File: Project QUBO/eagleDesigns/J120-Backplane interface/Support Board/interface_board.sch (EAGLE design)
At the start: 5 parts

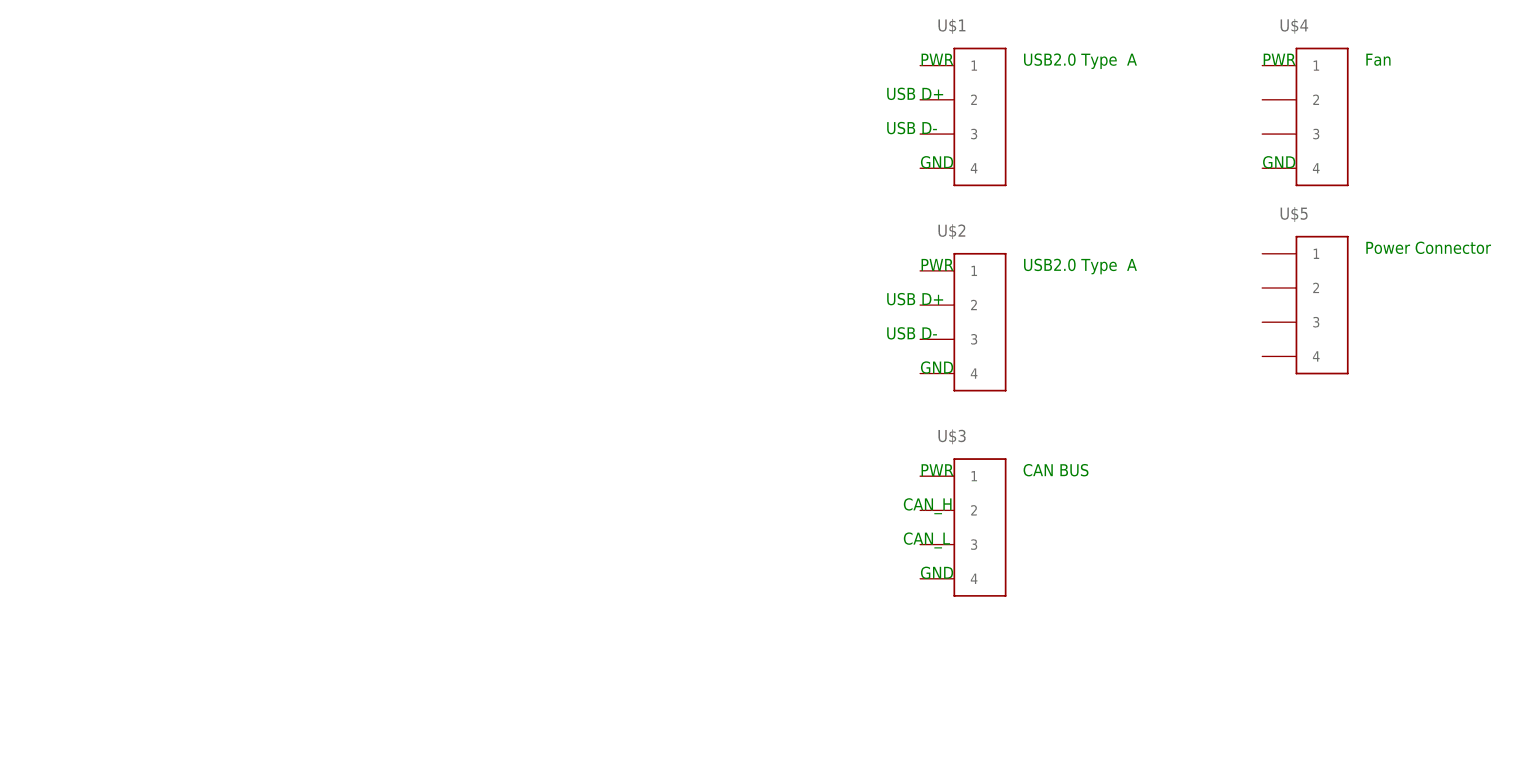
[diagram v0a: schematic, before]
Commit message: 
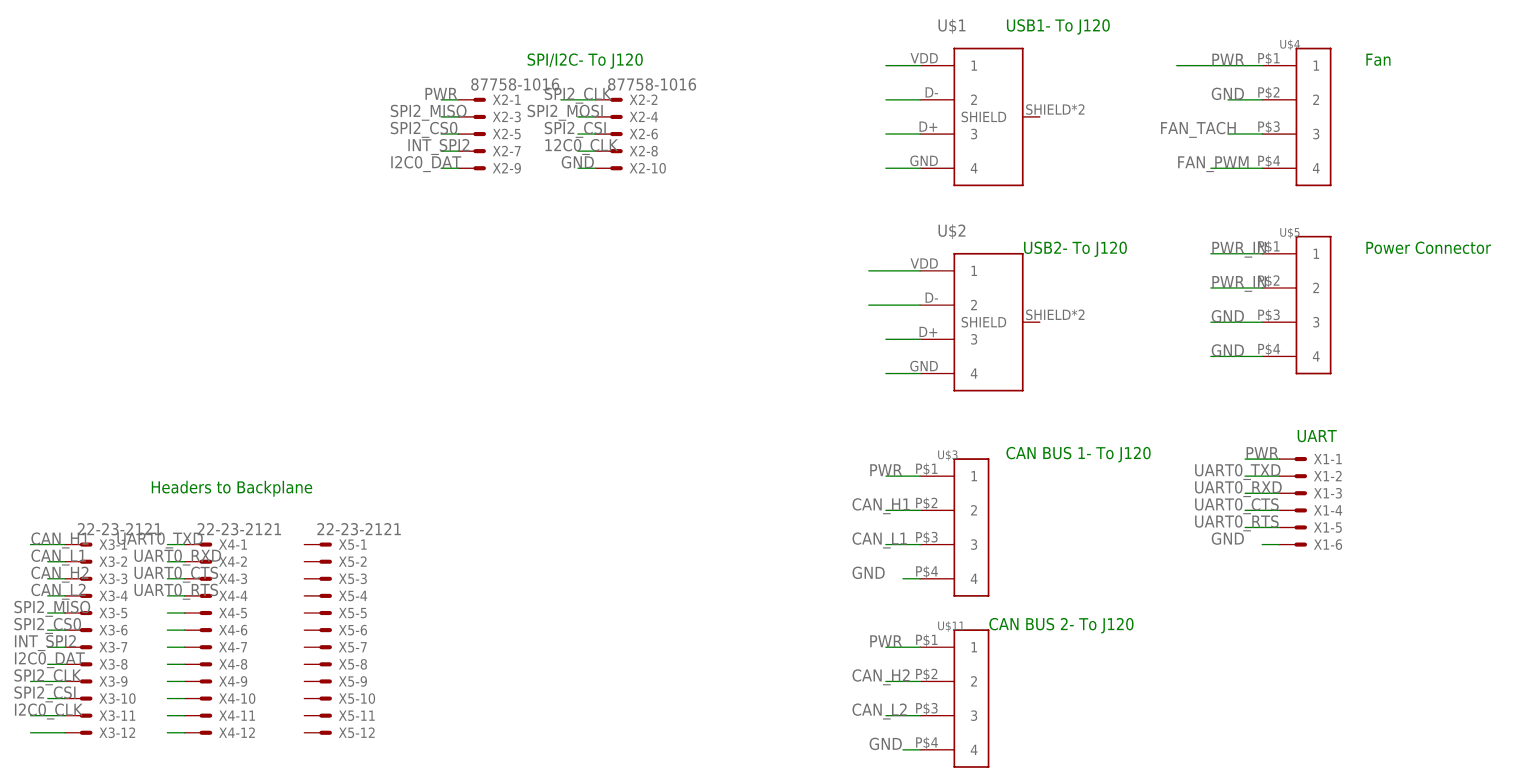
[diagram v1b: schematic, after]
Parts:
- added U$11: (no value), connectors:DF13-4
- added X1: (no value), con-molex_MOD:22-23-2061
- added X2: 87758-1016, con-molex_MOD:87758-1016
- added X3, X4, X5: 22-23-2121, con-molex_MOD:22-23-2121
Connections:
- new net 12C0_CLK: X2-8.S
- new net CAN_H1: U$3.2, X3-1.S
- new net CAN_H2: U$11.2, X3-3.S
- new net CAN_L1: U$3.3, X3-2.S
- new net CAN_L2: U$11.3, X3-4.S
- new net FAN_PWM: U$4.4
- new net FAN_TACH: U$4.3
- new net GND: U$1.4, U$11.4, U$2.4, U$3.4, U$4.2, U$5.3, U$5.4, X1-6.S, X2-10.S
- new net I2C0_CLK: X3-11.S
- new net I2C0_DAT: X2-9.S, X3-8.S
- new net INT_SPI2: X2-7.S, X3-7.S
- new net N$1: U$1.1
- new net N$10: X4-7.S
- new net N$11: X4-8.S
- new net N$12: X4-9.S
- new net N$13: X4-10.S
- new net N$14: X4-11.S
- new net N$15: X4-12.S
- new net N$19: X3-12.S
- new net N$2: U$1.2
- new net N$3: U$1.3
- new net N$8: X4-5.S
- new net N$9: X4-6.S
- new net PWR: U$11.1, U$2.1, U$3.1, U$4.1, X1-1.S, X2-1.S
- new net PWR_IN: U$5.1, U$5.2
- new net SPI2_CLK: X2-2.S, X3-9.S
- new net SPI2_CS0: X2-5.S, X3-6.S
- new net SPI2_CSI: X2-6.S, X3-10.S
- new net SPI2_MISO: X2-3.S, X3-5.S
- new net SPI2_MOSI: X2-4.S
- new net UART0_CTS: X1-4.S, X4-3.S
- new net UART0_RTS: X1-5.S, X4-4.S
- new net UART0_RXD: X1-3.S, X4-2.S
- new net UART0_TXD: X1-2.S, X4-1.S
- new net USB2_D+: U$2.3
- new net USB2_D-: U$2.2
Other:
- note added: "CAN BUS 1- To J120"
- note added: "CAN BUS 2- To J120"
- note added: "Headers to Backplane"
- note added: "SPI/I2C- To J120"
- note added: "UART"
- note added: "USB1- To J120"
- note added: "USB2- To J120"
- note removed: "CAN BUS"
- note removed: "CAN_H"
- note removed: "CAN_L"
- note removed: "GND"
- note removed: "PWR"
- note removed: "USB D+"
- note removed: "USB D-"
- note removed: "USB2.0 Type A"
